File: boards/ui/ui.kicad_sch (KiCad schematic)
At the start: 15 parts, among them J1 Conn_02x08_Counter_Clockwise, J2 Conn_02x08_Counter_Clockwise, J3 Conn_02x08_Counter_Clockwise, J4 Conn_02x08_Counter_Clockwise, J5 Conn_02x04_Counter_Clockwise, J7 Conn_02x08_Counter_Clockwise

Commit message: Updated UI board connector positions
https://github.com/shmoergh/hog/issues/31

Moving the tuner trimmers on the Core board required to reposition the connector headers too. This also had to be done on the UI board otherwise it won't be possible to connect the two boards.
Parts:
- J1, J2, J3, J4: footprint Connector_IDC:IDC-Header_2x08_P2.54mm_Vertical -> Connector_PinHeader_2.54mm:PinHeader_2x08_P2.54mm_Vertical
- J_POWER1: footprint Connector_IDC:IDC-Header_2x05_P2.54mm_Vertical -> Connector_PinHeader_2.54mm:PinHeader_2x05_P2.54mm_Vertical
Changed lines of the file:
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@@
 			)
 		)
-		(property "Footprint" "Connector_IDC:IDC-Header_2x08_P2.54mm_Vertical"
+		(property "Footprint" "Connector_PinHeader_2.54mm:PinHeader_2x08_P2.54mm_Vertical"
 			(at 364.49 39.37 0)
 			(effects
@@
 			)
 		)
-		(property "Footprint" "Connector_IDC:IDC-Header_2x05_P2.54mm_Vertical"
+		(property "Footprint" "Connector_PinHeader_2.54mm:PinHeader_2x05_P2.54mm_Vertical"
 			(at 364.49 102.87 0)
 			(effects
@@
 			)
 		)
-		(property "Footprint" "Connector_IDC:IDC-Header_2x08_P2.54mm_Vertical"
+		(property "Footprint" "Connector_PinHeader_2.54mm:PinHeader_2x08_P2.54mm_Vertical"
 			(at 312.42 71.12 0)
 			(effects
@@
 			)
 		)
-		(property "Footprint" "Connector_IDC:IDC-Header_2x08_P2.54mm_Vertical"
+		(property "Footprint" "Connector_PinHeader_2.54mm:PinHeader_2x08_P2.54mm_Vertical"
 			(at 312.42 39.37 0)
 			(effects
@@
 			)
 		)
-		(property "Footprint" "Connector_IDC:IDC-Header_2x08_P2.54mm_Vertical"
+		(property "Footprint" "Connector_PinHeader_2.54mm:PinHeader_2x08_P2.54mm_Vertical"
 			(at 312.42 106.68 0)
 			(effects

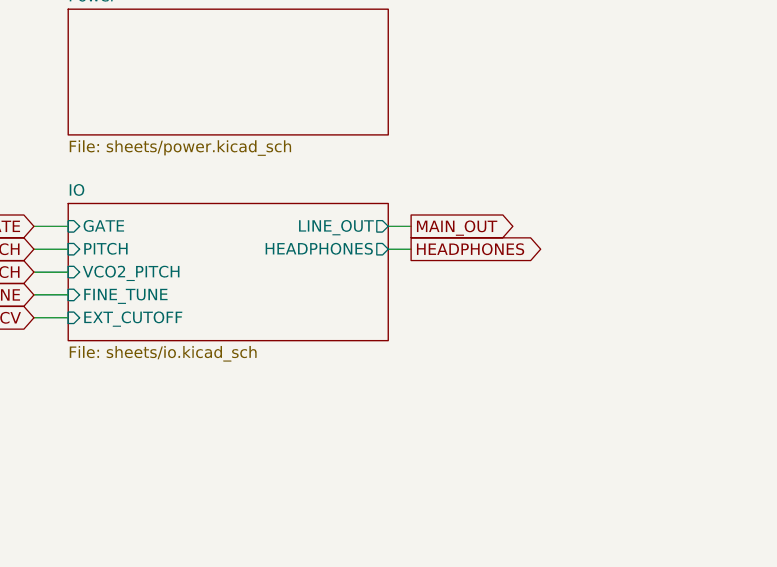
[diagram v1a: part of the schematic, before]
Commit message: Replaced wired MIDI connection to pins
https://github.com/shmoergh/hog/issues/32

MIDI connection was done with manual wired NTS connectors. Now they are replaced with pins and pinheaders just like the other boards.
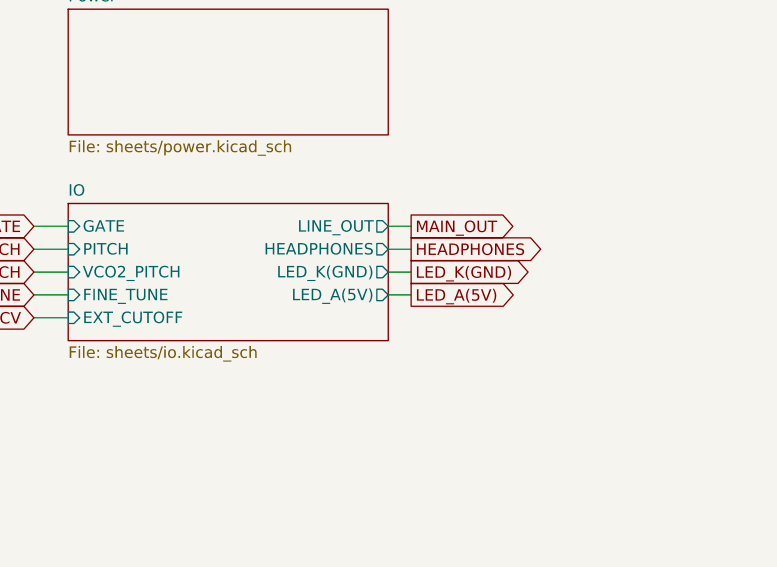
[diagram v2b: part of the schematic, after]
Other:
- sheet IO ports: added LED_A(5V), LED_K(GND); removed none
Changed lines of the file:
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@@
 	(wire
 		(pts
+			(xy 459.74 106.68) (xy 462.28 106.68)
+		)
+		(stroke
+			(width 0)
+			(type default)
+		)
+	)
+	(wire
+		(pts
 			(xy 412.75 26.67) (xy 412.75 31.75)
 		)
@@
 		)
 	)
+	(wire
+		(pts
+			(xy 459.74 109.22) (xy 462.28 109.22)
+		)
+		(stroke
+			(width 0)
+			(type default)
+		)
+	)
 	(text "DONE"
 		(exclude_from_sim no)
@@
 		)
 	)
+	(global_label "LED_A(5V)"
+		(shape output)
+		(at 462.28 109.22 0)
+		(fields_autoplaced yes)
+		(effects
+			(font
+				(size 1.27 1.27)
+			)
+			(justify left)
+		)
+		(property "Intersheetrefs" "${INTERSHEET_REFS}"
+			(at 474.76 109.22 0)
+			(effects
+				(font
+					(size 1.27 1.27)
+				)
+				(justify left)
+				(hide yes)
+			)
+		)
+	)
 	(global_label "FINE_TUNE"
 		(shape input)
@@
 		)
 	)
+	(global_label "LED_K(GND)"
+		(shape output)
+		(at 462.28 106.68 0)
+		(fields_autoplaced yes)
+		(effects
+			(font
+				(size 1.27 1.27)
+			)
+			(justify left)
+		)
+		(property "Intersheetrefs" "${INTERSHEET_REFS}"
+			(at 476.5138 106.68 0)
+			(effects
+				(font
+					(size 1.27 1.27)
+				)
+				(justify left)
+				(hide yes)
+			)
+		)
+	)
 	(global_label "DECAY"
 		(shape output)
@@
 			)
 		)
+		(pin "LED_K(GND)" output
+			(at 459.74 106.68 0)
+			(effects
+				(font
+					(size 1.27 1.27)
+				)
+				(justify right)
+			)
+		)
+		(pin "LED_A(5V)" output
+			(at 459.74 109.22 0)
+			(effects
+				(font
+					(size 1.27 1.27)
+				)
+				(justify right)
+			)
+		)

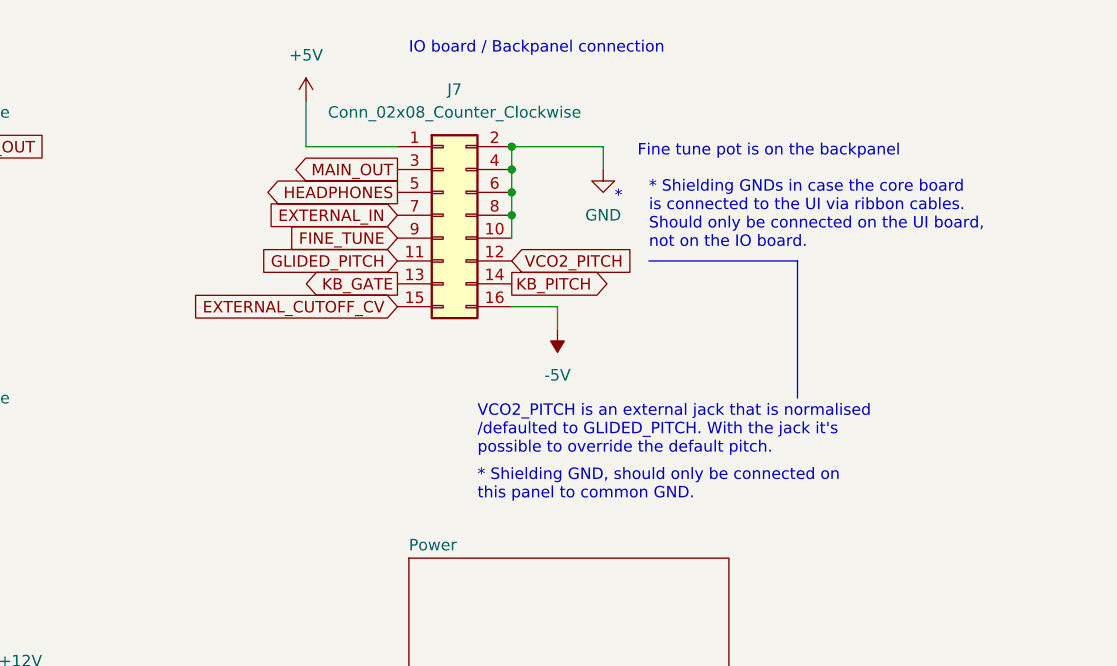
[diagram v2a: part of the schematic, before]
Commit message: Removed backpanel IO conn. + fixed drone voltage
https://github.com/shmoergh/hog/issues/37
The IO back panel connector on the UI board is a leftover from an earlier prototype. Can be removed.

https://github.com/shmoergh/hog/issues/36
ATM the gate voltage for drone mode is fixed to 5V which makes it quieter than the normal gate. Drone mode gate voltage should be 8V.
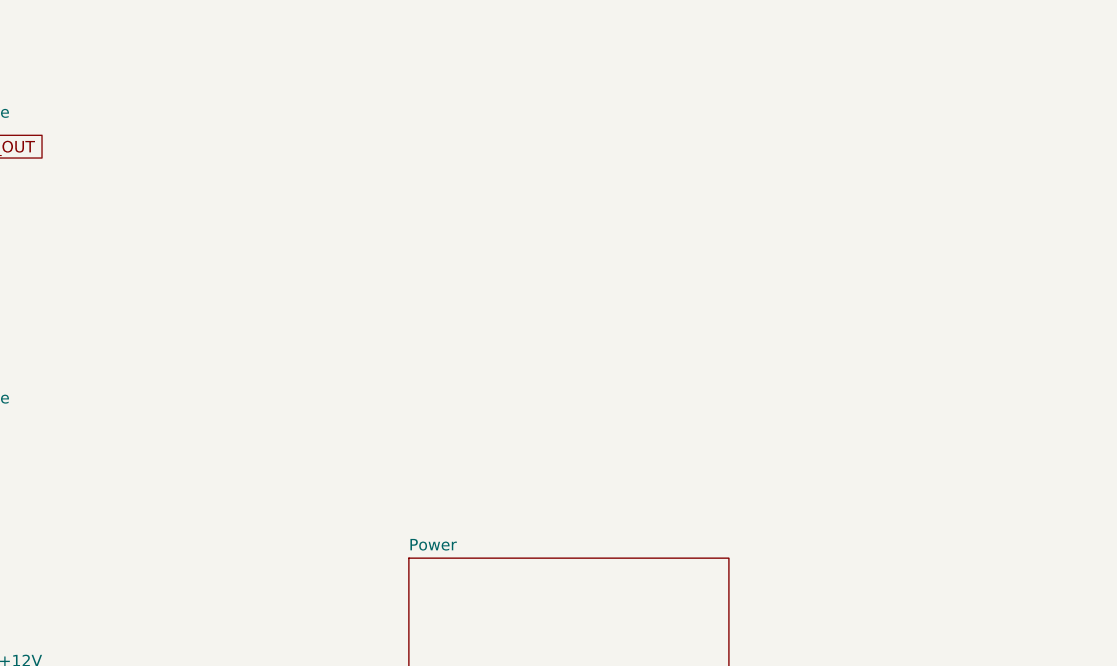
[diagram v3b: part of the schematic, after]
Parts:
- removed J7: Conn_02x08_Counter_Clockwise, Connector_PinHeader_2.54mm:PinHeader_2x08_P2.54mm_Vertical, symbol Connector_Generic:Conn_02x08_Odd_Even
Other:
- note removed: "*"
- note removed: "* Shielding GND, should only be connected on this panel to common GND."
- note removed: "* Shielding GNDs in case the core board is connected to the UI via ribbon cables. Should only be connected on the UI board, not on the IO board."
- note removed: "Fine tune pot is on the backpanel"
- note removed: "IO board / Backpanel connection"
- note removed: "VCO2_PITCH is an external jack that is normalised /defaulted to GLIDED_PITCH. With the jack it's possible to override the default pitch."

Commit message: Added production files for the UI board
ref https://github.com/shmoergh/hog/issues/19
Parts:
- J1, J2, J3, J4: Part No. (none) -> 649-1012938191601BLF; Part URL (none) -> https://mou.sr/3ZS3vh3; Vendor (none) -> Mouser; now in the parts list
- J5: Part No. (none) -> 737-PH2-08-UA; Part URL (none) -> https://mou.sr/4gxLnib; Vendor (none) -> Mouser; now in the parts list
- J_POWER1: Part No. (none) -> 737-PH2-10-UA; Part URL (none) -> https://mou.sr/3D13TAT; Vendor (none) -> Mouser; now in the parts list
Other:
- note added: "Checked"
